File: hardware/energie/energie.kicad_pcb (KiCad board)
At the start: 2 copper layers, 102 x 87 mm, 88 parts, among them J1 transfos, J2 Conn_01x05_Pin, J3 linky, J4 Serial, J5 pilotes, J6 gpio, J7 I2C, J8 power, J9 ACin, Q1 BSS123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

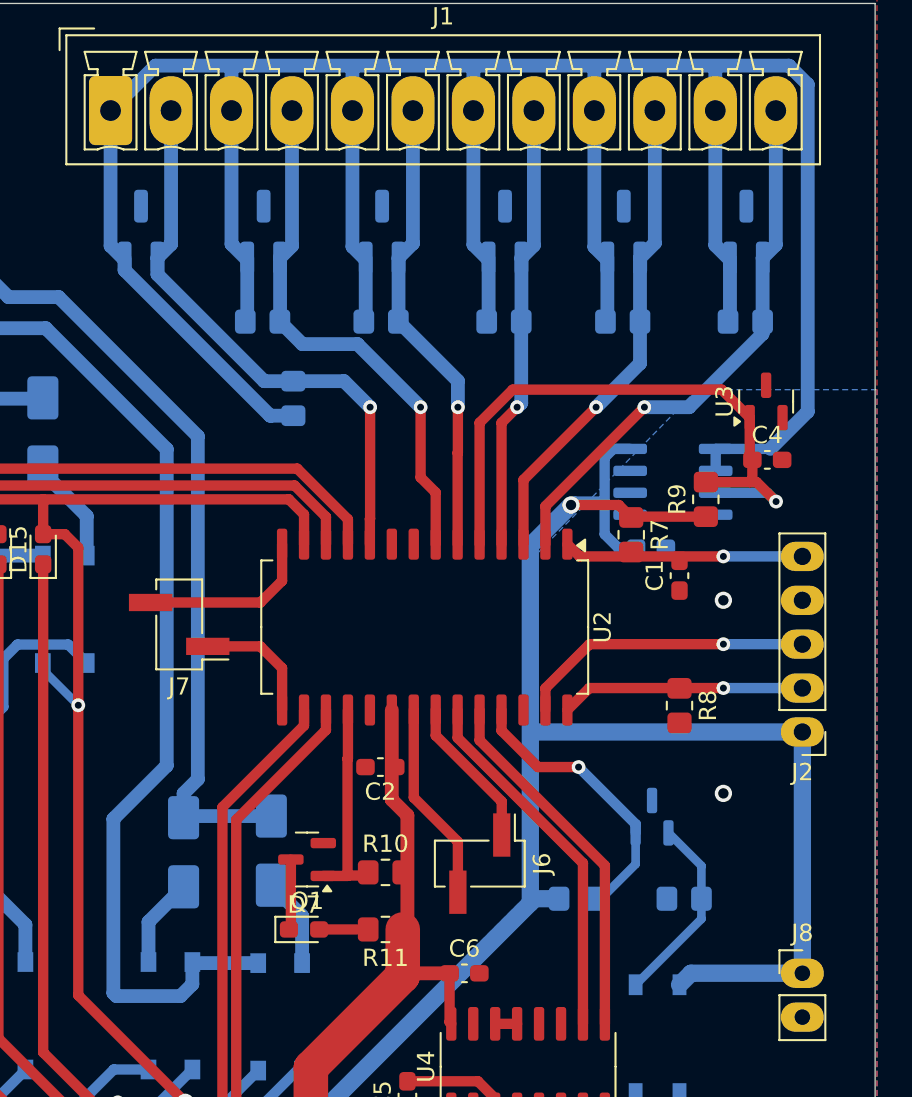
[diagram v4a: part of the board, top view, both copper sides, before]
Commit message: Energie: mesure de courant ajout d'une resistance de protection serie sur les entrees pic18
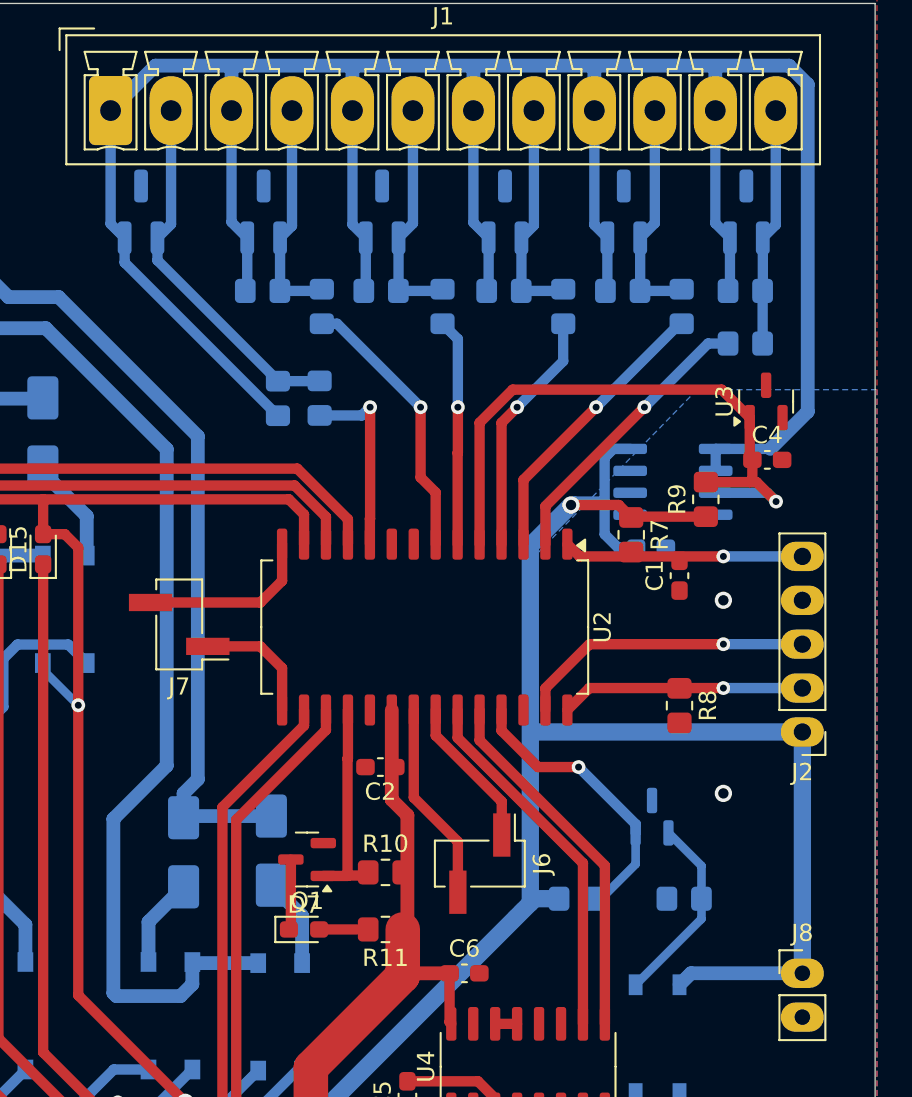
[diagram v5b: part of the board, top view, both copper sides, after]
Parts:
- added R21: 330, Resistor_SMD:R_0805_2012Metric_Pad1.20x1.40mm_HandSolder, B.Cu at (170.7, 70.5)
- added R22: 330, Resistor_SMD:R_0805_2012Metric_Pad1.20x1.40mm_HandSolder, B.Cu at (167.0, 68.3)
- added R23: 330, Resistor_SMD:R_0805_2012Metric_Pad1.20x1.40mm_HandSolder, B.Cu at (160.1, 68.3)
- added R24: 330, Resistor_SMD:R_0805_2012Metric_Pad1.20x1.40mm_HandSolder, B.Cu at (153.2, 68.3)
- added R25: 330, Resistor_SMD:R_0805_2012Metric_Pad1.20x1.40mm_HandSolder, B.Cu at (146.2, 68.3)
- added R26: 330, Resistor_SMD:R_0805_2012Metric_Pad1.20x1.40mm_HandSolder, B.Cu at (146.1, 73.6)
- moved R2 1.78 mm to (142.7, 67.4)
- moved R3 1.78 mm to (149.6, 67.4)
- moved R4 1.78 mm to (156.7, 67.4)
- moved R5 1.78 mm to (163.6, 67.4)
- moved R6 1.78 mm to (170.7, 67.4)
- moved D1 1.17 mm to (135.7, 62.9)
- moved D2 1.17 mm to (142.8, 62.9)
- moved D3 1.17 mm to (149.7, 62.9)
- moved D4 1.17 mm to (156.8, 62.9)
- moved D5 1.17 mm to (163.7, 62.9)
- moved D6 1.17 mm to (170.7, 62.9)
- moved R1 0.89 mm to (143.6, 73.7)
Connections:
- U2 pad 10: Net-(J1-Pin_2) -> Net-(U2-RA6/OSC2/CLKOUT)
- U2 pad 2: Net-(J1-Pin_12) -> Net-(U2-RA0/CxIN0-)
- U2 pad 3: Net-(J1-Pin_10) -> Net-(U2-RA1/CxIN1-)
- U2 pad 4: Net-(J1-Pin_8) -> Net-(U2-RA2/Vref-/DAC1OUT1/CxIN0+)
- U2 pad 6: Net-(J1-Pin_6) -> Net-(U2-RA4)
- U2 pad 7: Net-(J1-Pin_4) -> Net-(U2-RA5)
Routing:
- net Net-(J1-Pin_12): track 32.1 -> 13.8 mm, vias 1 -> 0
- net Net-(J1-Pin_4): track 31.0 -> 13.2 mm, vias 1 -> 0
- net Net-(U2-RA0/CxIN0-): track 0.00 -> 16.7 mm, vias 0 -> 1
- net Net-(U2-RA1/CxIN1-): track 0.00 -> 16.6 mm, vias 0 -> 1
- net Net-(U2-RA5): track 0.00 -> 16.0 mm, vias 0 -> 1
- net Net-(J1-Pin_10): track 28.2 -> 13.2 mm, vias 1 -> 0
- net Net-(U2-RA2/Vref-/DAC1OUT1/CxIN0+): track 0.00 -> 14.2 mm, vias 0 -> 1
- net Net-(J1-Pin_6): track 26.9 -> 13.4 mm, vias 1 -> 0
- net Net-(U2-RA4): track 0.00 -> 13.1 mm, vias 0 -> 1
- net Net-(J1-Pin_8): track 25.9 -> 13.2 mm, vias 1 -> 0
- net Net-(J1-Pin_2): track 33.2 -> 20.8 mm, vias 1 -> 0
- net Net-(U2-RA6/OSC2/CLKOUT): track 0.00 -> 11.0 mm, vias 0 -> 1
- net Net-(J1-Pin_1): track 165.8 -> 156.8 mm

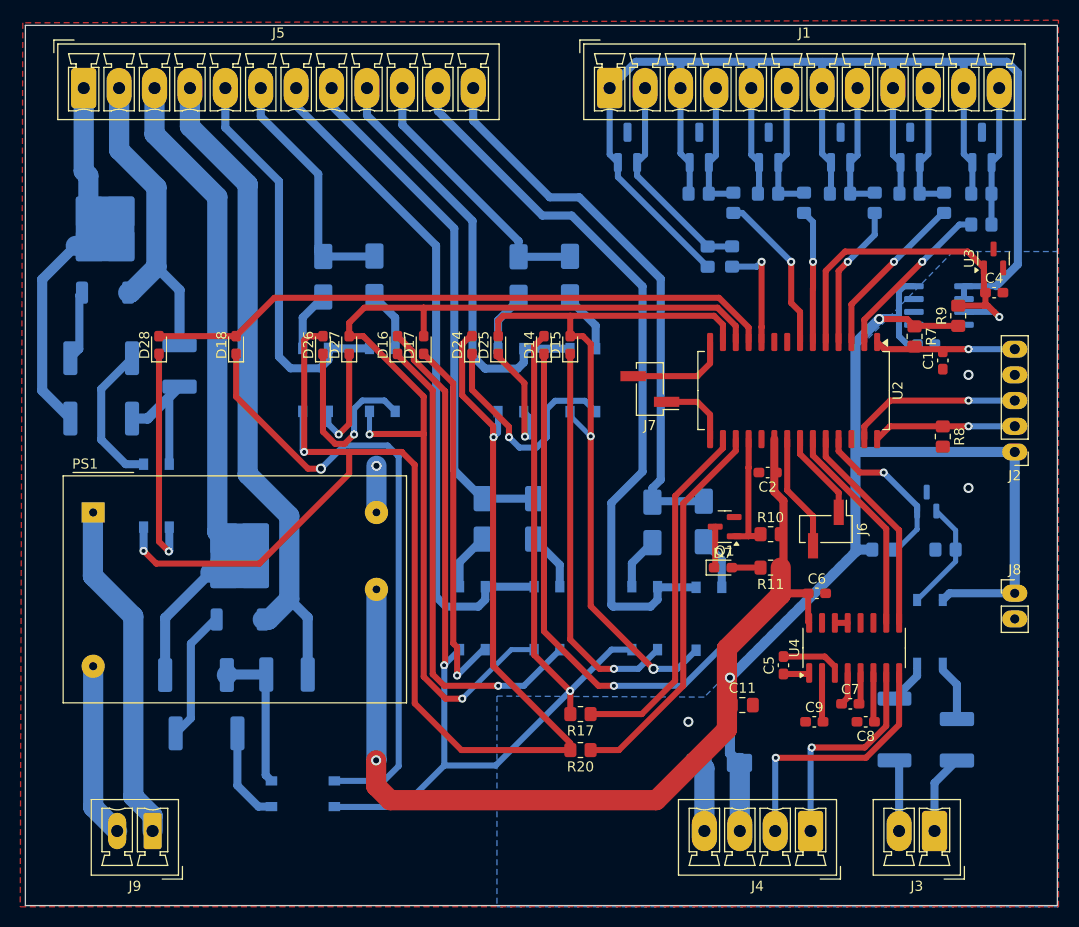
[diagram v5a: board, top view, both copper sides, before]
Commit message: Fix Q2 wiring, it was reversed Fix U5 footprint Fix C10 and similar footprints
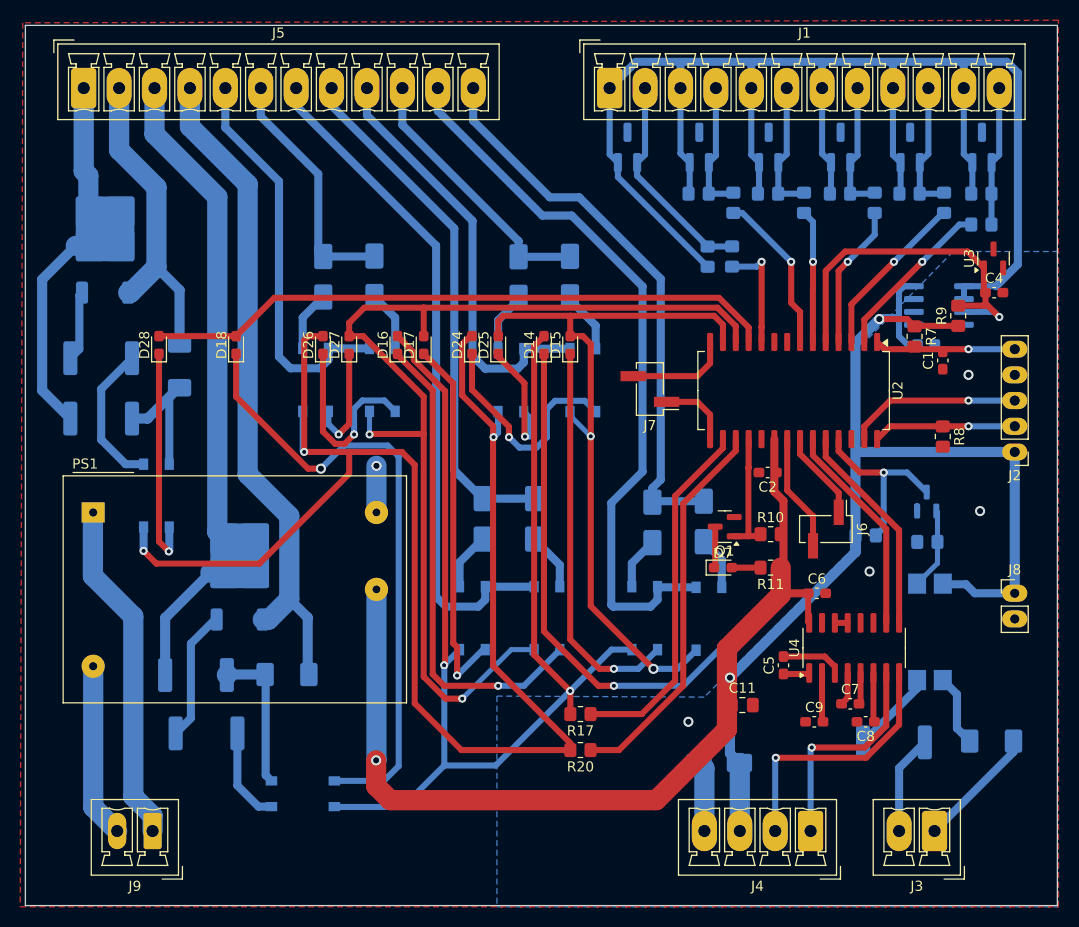
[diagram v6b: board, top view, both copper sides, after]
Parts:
- C10, C12, C13: footprint Capacitor_SMD:C_1812_4532Metric -> local:C_1808_4520Metric_Pad1.72x2.30mm_HandSolder
- PS1: value IRM-02-5 -> IRM-01-5
- U5: footprint Package_SO:MFSOP6-4_4.4x3.6mm_P1.27mm -> Package_DIP:SMDIP-4_W9.53mm
- moved C10 3.43 mm to (171.7, 121.5), turned to 180 degrees
- moved R12 2.16 mm to (159.3, 101.2)
- moved R13 1.95 mm to (165.4, 101.9)
- moved R14 1.27 mm to (162.1, 121.7), turned to 0 degrees
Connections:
- Q2 pad 2: Net-(Q2-S) -> GND
- Q2 pad 3: GND -> Net-(Q2-D)
- R12 pad 2: Net-(Q2-S) -> Net-(Q2-D)
- U2 pad 25: Net-(Q2-S) -> Net-(Q2-D)
- U5 pad 3: Net-(R14-Pad1) -> Net-(Q2-G)
- U5 pad 4: Net-(Q2-G) -> +5V
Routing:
- net Net-(Q2-D): track 0.00 -> 18.1 mm, vias 0 -> 1
- net Net-(Q2-S): track 16.3 -> 0.00 mm, vias 1 -> 0
- net Net-(R14-Pad1): track 3.72 -> 8.37 mm
- net Net-(J3-Pin_1): track 7.88 -> 12.1 mm
- net Net-(Q2-G): track 11.2 -> 8.05 mm
- net Net-(J3-Pin_2): track 7.17 -> 9.82 mm
- net Net-(C10-Pad2): track 5.39 -> 7.13 mm
- net Net-(J1-Pin_1): track 156.8 -> 156.0 mm
- net GND: track 11.6 -> 12.1 mm, vias 4 -> 5
